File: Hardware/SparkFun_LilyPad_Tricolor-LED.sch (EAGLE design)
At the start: 13 parts

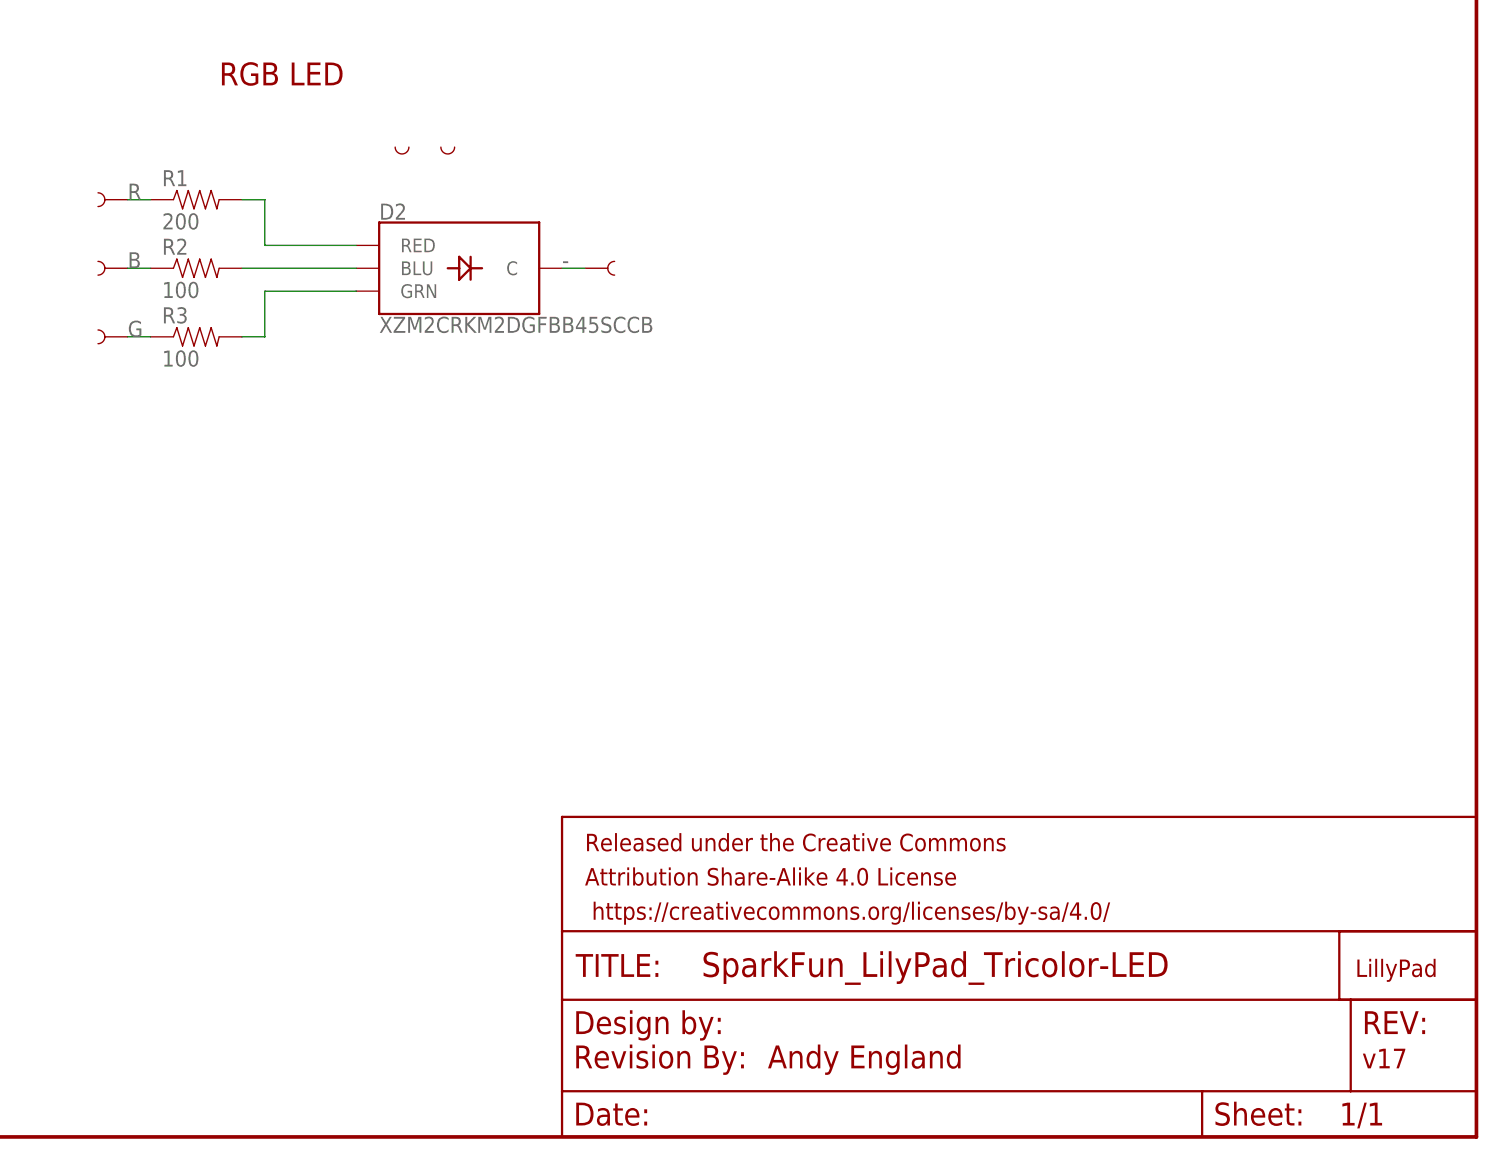
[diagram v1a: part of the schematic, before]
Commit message: revising to common cathode
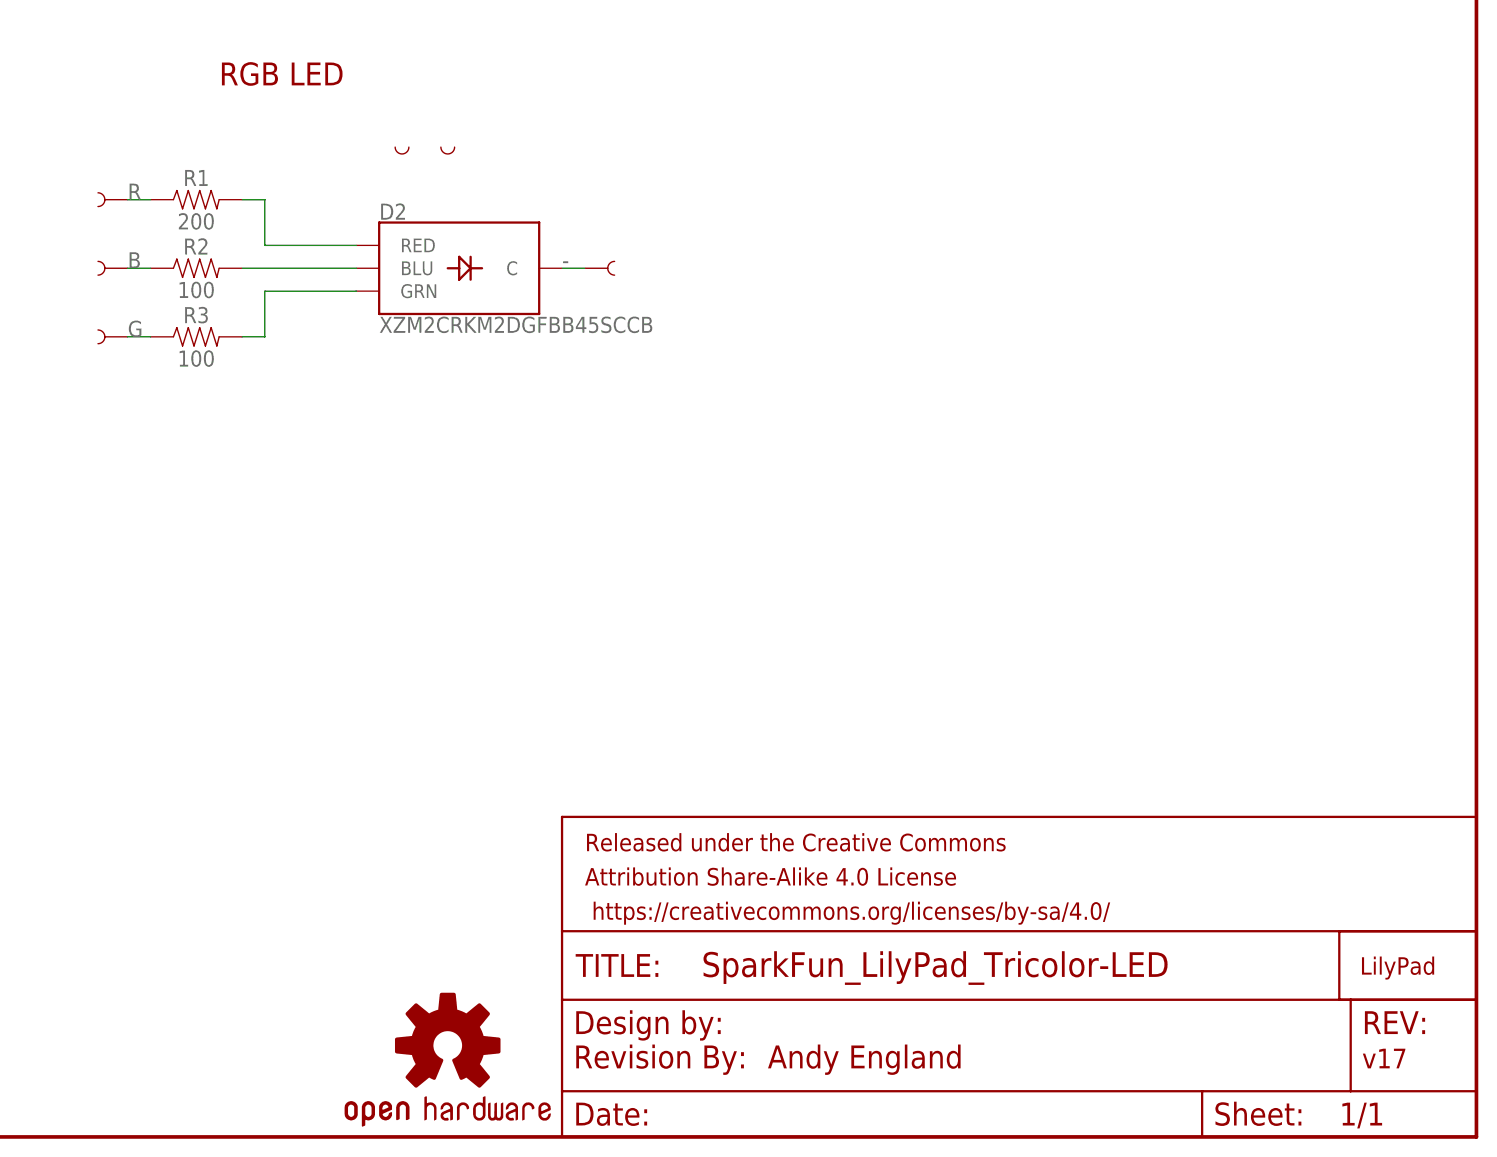
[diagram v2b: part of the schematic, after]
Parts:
- added LOGO2: OSHW-LOGOS, SparkFun-Aesthetics:OSHW-LOGOS
- R1: device SparkFun:RESISTOR0402-RES -> SparkFun-Resistors:200OHM-0603-1/10W-1%
- R2, R3: device SparkFun:RESISTOR0402-RES -> SparkFun-Resistors:100OHM-0603-1/10W-1%
- U$1: value LOGO-LPL -> LOGO-LPLP; device LilyPad-Wearables:LOGO-LPL -> SparkFun-Retired:LOGO-LPLP
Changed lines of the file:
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@@
 </classes>
 <parts>
-<part name="R1" library="SparkFun" deviceset="RESISTOR" device="0402-RES" value="200"/>
-<part name="R2" library="SparkFun" deviceset="RESISTOR" device="0402-RES" value="100"/>
-<part name="R3" library="SparkFun" deviceset="RESISTOR" device="0402-RES" value="100"/>
+<part name="R1" library="SparkFun-Resistors" deviceset="200OHM" device="-0603-1/10W-1%" value="200"/>
+<part name="R2" library="SparkFun-Resistors" deviceset="100OHM" device="-0603-1/10W-1%" value="100"/>
+<part name="R3" library="SparkFun-Resistors" deviceset="100OHM" device="-0603-1/10W-1%" value="100"/>
 <part name="FRAME1" library="SparkFun-Aesthetics" deviceset="FRAME-LETTER" device=""/>
 <part name="U$7" library="LilyPad-Wearables" deviceset="SEWTAP" device="6"/>
@@
 <part name="U$2" library="LilyPad-Wearables" deviceset="SEWTAP-NOHOLE" device="2"/>
 <part name="U$3" library="LilyPad-Wearables" deviceset="SEWTAP-NOHOLE" device="2"/>
-<part name="U$1" library="LilyPad-Wearables" deviceset="LOGO-LP" device="L"/>
+<part name="U$1" library="SparkFun-Retired" deviceset="LOGO-LP" device="LP"/>
 <part name="D2" library="SparkFun-LED" deviceset="SUNLED" device="SMD1" value="XZM2CRKM2DGFBB45SCCB"/>
 <part name="LOGO1" library="SparkFun-Aesthetics" deviceset="REVISION" device=""/>
+<part name="LOGO2" library="SparkFun-Aesthetics" deviceset="OSHW-LOGO" device="S"/>
 </parts>
 <sheets>
@@
 <instance part="D2" gate="G1" x="134.62" y="96.52"/>
 <instance part="LOGO1" gate="G$1" x="148.59" y="7.62"/>
+<instance part="LOGO2" gate="G$1" x="134.62" y="10.16"/>
 </instances>
 <busses>

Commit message: updating
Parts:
- added FD1, FD2, FD3, FD4: FIDUCIAL1X2, SparkFun-Aesthetics:FIDUCIAL1X2
- added LOGO3: SFE_LOGO_FLAME.1_INCH, SparkFun-Aesthetics:SFE_LOGO_FLAME.1_INCH
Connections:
- net - renamed GND
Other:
- note added: "Dia Williams"
- note added: "VCC Range: Red: 2.2V-12V Green: 2.8V-6V Blue: 2.8V-6V"
- note added: "v20"
- note removed: "v17"
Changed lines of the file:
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@@
 <?xml version="1.0" encoding="utf-8"?>
 <!DOCTYPE eagle SYSTEM "eagle.dtd">
-<eagle version="9.0.1">
+<eagle version="9.1.0">
 <drawing>
 <settings>
@@
 <part name="LOGO1" library="SparkFun-Aesthetics" deviceset="REVISION" device=""/>
 <part name="LOGO2" library="SparkFun-Aesthetics" deviceset="OSHW-LOGO" device="S"/>
+<part name="LOGO3" library="SparkFun-Aesthetics" deviceset="SFE_LOGO_FLAME" device=".1_INCH" value="SFE_LOGO_FLAME.1_INCH"/>
+<part name="GND1" library="SparkFun-PowerSymbols" deviceset="GND" device=""/>
+<part name="FD1" library="SparkFun-Aesthetics" deviceset="FIDUCIAL" device="1X2"/>
+<part name="FD2" library="SparkFun-Aesthetics" deviceset="FIDUCIAL" device="1X2"/>
+<part name="FD3" library="SparkFun-Aesthetics" deviceset="FIDUCIAL" device="1X2"/>
+<part name="FD4" library="SparkFun-Aesthetics" deviceset="FIDUCIAL" device="1X2"/>
 </parts>
 <sheets>
 <sheet>
 <plain>
-<text x="236.22" y="7.62" size="2.1844" layer="94" font="vector">v17</text>
+<text x="236.22" y="7.62" size="2.1844" layer="94" font="vector">v20</text>
 <text x="170.18" y="7.62" size="2.54" layer="94" font="vector">Andy England</text>
-<text x="109.22" y="116.84" size="2.54" layer="94" font="vector">RGB LED</text>
+<text x="109.22" y="121.92" size="2.54" layer="94" font="vector">RGB LED</text>
+<text x="166.37" y="11.43" size="2.54" layer="94" font="vector">Dia Williams</text>
+<text x="109.22" y="114.3" size="1.27" layer="97" font="vector" ratio="15">VCC Range:
+Red: 2.2V-12V
+Green: 2.8V-6V
+Blue: 2.8V-6V</text>
 </plain>
 <instances>
@@
 <instance part="FRAME1" gate="G$1" x="0" y="0"/>
 <instance part="FRAME1" gate="V" x="147.32" y="0"/>
-<instance part="U$7" gate="G$1" x="96.52" y="104.14" rot="R180"/>
-<instance part="U$8" gate="G$1" x="96.52" y="88.9" rot="R180"/>
-<instance part="U$9" gate="G$1" x="96.52" y="96.52" rot="R180"/>
-<instance part="U$10" gate="G$1" x="152.4" y="96.52"/>
+<instance part="U$7" gate="G$1" x="99.06" y="99.06" rot="R270"/>
+<instance part="U$8" gate="G$1" x="99.06" y="83.82" rot="R270"/>
+<instance part="U$9" gate="G$1" x="99.06" y="91.44" rot="R270"/>
+<instance part="U$10" gate="G$1" x="167.64" y="96.52"/>
 <instance part="U$2" gate="G$1" x="129.54" y="109.22" rot="R90"/>
 <instance part="U$3" gate="G$1" x="134.62" y="109.22" rot="R90"/>
@@
 <instance part="LOGO1" gate="G$1" x="148.59" y="7.62"/>
 <instance part="LOGO2" gate="G$1" x="134.62" y="10.16"/>
+<instance part="LOGO3" gate="G$1" x="114.3" y="2.54"/>
+<instance part="GND1" gate="1" x="162.56" y="91.44"/>
+<instance part="FD1" gate="G$1" x="238.76" y="30.48"/>
+<instance part="FD2" gate="G$1" x="241.3" y="30.48"/>
+<instance part="FD3" gate="G$1" x="241.3" y="27.94"/>
+<instance part="FD4" gate="G$1" x="238.76" y="27.94"/>
 </instances>
 <busses>
@@
 </segment>
 </net>
-<net name="-" class="0">
-<segment>
-<wire x1="149.86" y1="96.52" x2="147.32" y2="96.52" width="0.1524" layer="91"/>
-<label x="147.32" y="96.52" size="1.778" layer="95"/>
+<net name="G" class="0">
+<segment>
+<pinref part="R3" gate="G$1" pin="1"/>
+<wire x1="101.6" y1="88.9" x2="99.06" y2="88.9" width="0.1524" layer="91"/>
+<pinref part="U$8" gate="G$1" pin="1"/>
+<wire x1="99.06" y1="88.9" x2="96.52" y2="88.9" width="0.1524" layer="91"/>
+<wire x1="99.06" y1="86.36" x2="99.06" y2="88.9" width="0.1524" layer="91"/>
+<junction x="99.06" y="88.9"/>
+<label x="96.52" y="88.9" size="1.27" layer="95" font="vector" rot="R180" xref="yes"/>
+</segment>
+</net>
+<net name="B" class="0">
+<segment>
+<pinref part="U$9" gate="G$1" pin="1"/>
+<wire x1="99.06" y1="93.98" x2="99.06" y2="96.52" width="0.1524" layer="91"/>
+<pinref part="R2" gate="G$1" pin="1"/>
+<wire x1="99.06" y1="96.52" x2="101.6" y2="96.52" width="0.1524" layer="91"/>
+<wire x1="99.06" y1="96.52" x2="96.52" y2="96.52" width="0.1524" layer="91"/>
+<junction x="99.06" y="96.52"/>
+<label x="96.52" y="96.52" size="1.27" layer="95" font="vector" rot="R180" xref="yes"/>
+</segment>
+</net>
+<net name="R" class="0">
+<segment>
+<pinref part="R1" gate="G$1" pin="1"/>
+<wire x1="96.52" y1="104.14" x2="99.06" y2="104.14" width="0.1524" layer="91"/>
+<pinref part="U$7" gate="G$1" pin="1"/>
+<wire x1="99.06" y1="104.14" x2="101.6" y2="104.14" width="0.1524" layer="91"/>
+<wire x1="99.06" y1="101.6" x2="99.06" y2="104.14" width="0.1524" layer="91"/>
+<junction x="99.06" y="104.14"/>
+<label x="96.52" y="104.14" size="1.27" layer="95" font="vector" rot="R180" xref="yes"/>
+</segment>
+</net>
+<net name="GND" class="0">
+<segment>
+<pinref part="D2" gate="G1" pin="C"/>
+<wire x1="147.32" y1="96.52" x2="162.56" y2="96.52" width="0.1524" layer="91"/>
 <pinref part="U$10" gate="G$1" pin="1"/>
-<pinref part="D2" gate="G1" pin="C"/>
-</segment>
-</net>
-<net name="R" class="0">
-<segment>
-<wire x1="99.06" y1="104.14" x2="101.6" y2="104.14" width="0.1524" layer="91"/>
-<label x="99.06" y="104.14" size="1.778" layer="95"/>
-<pinref part="R1" gate="G$1" pin="1"/>
-<pinref part="U$7" gate="G$1" pin="1"/>
-</segment>
-</net>
-<net name="B" class="0">
-<segment>
-<wire x1="99.06" y1="96.52" x2="101.6" y2="96.52" width="0.1524" layer="91"/>
-<label x="99.06" y="96.52" size="1.778" layer="95"/>
-<pinref part="R2" gate="G$1" pin="1"/>
-<pinref part="U$9" gate="G$1" pin="1"/>
-</segment>
-</net>
-<net name="G" class="0">
-<segment>
-<wire x1="99.06" y1="88.9" x2="101.6" y2="88.9" width="0.1524" layer="91"/>
-<label x="99.06" y="88.9" size="1.778" layer="95"/>
-<pinref part="R3" gate="G$1" pin="1"/>
-<pinref part="U$8" gate="G$1" pin="1"/>
+<wire x1="165.1" y1="96.52" x2="162.56" y2="96.52" width="0.1524" layer="91"/>
+<pinref part="GND1" gate="1" pin="GND"/>
+<wire x1="162.56" y1="93.98" x2="162.56" y2="96.52" width="0.1524" layer="91"/>
+<junction x="162.56" y="96.52"/>
 </segment>
 </net>
@@
 </schematic>
 </drawing>
+<compatibility>
+<note version="6.3" minversion="6.2.2" severity="warning">
+Since Version 6.2.2 text objects can contain more than one line,
+which will not be processed correctly with this version.
+</note>
+</compatibility>
 </eagle>
